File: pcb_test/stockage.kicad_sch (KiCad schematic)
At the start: 53 parts, among them U6 IS21EF08G-JCLI, U7 MX66LM1G45GXDI00

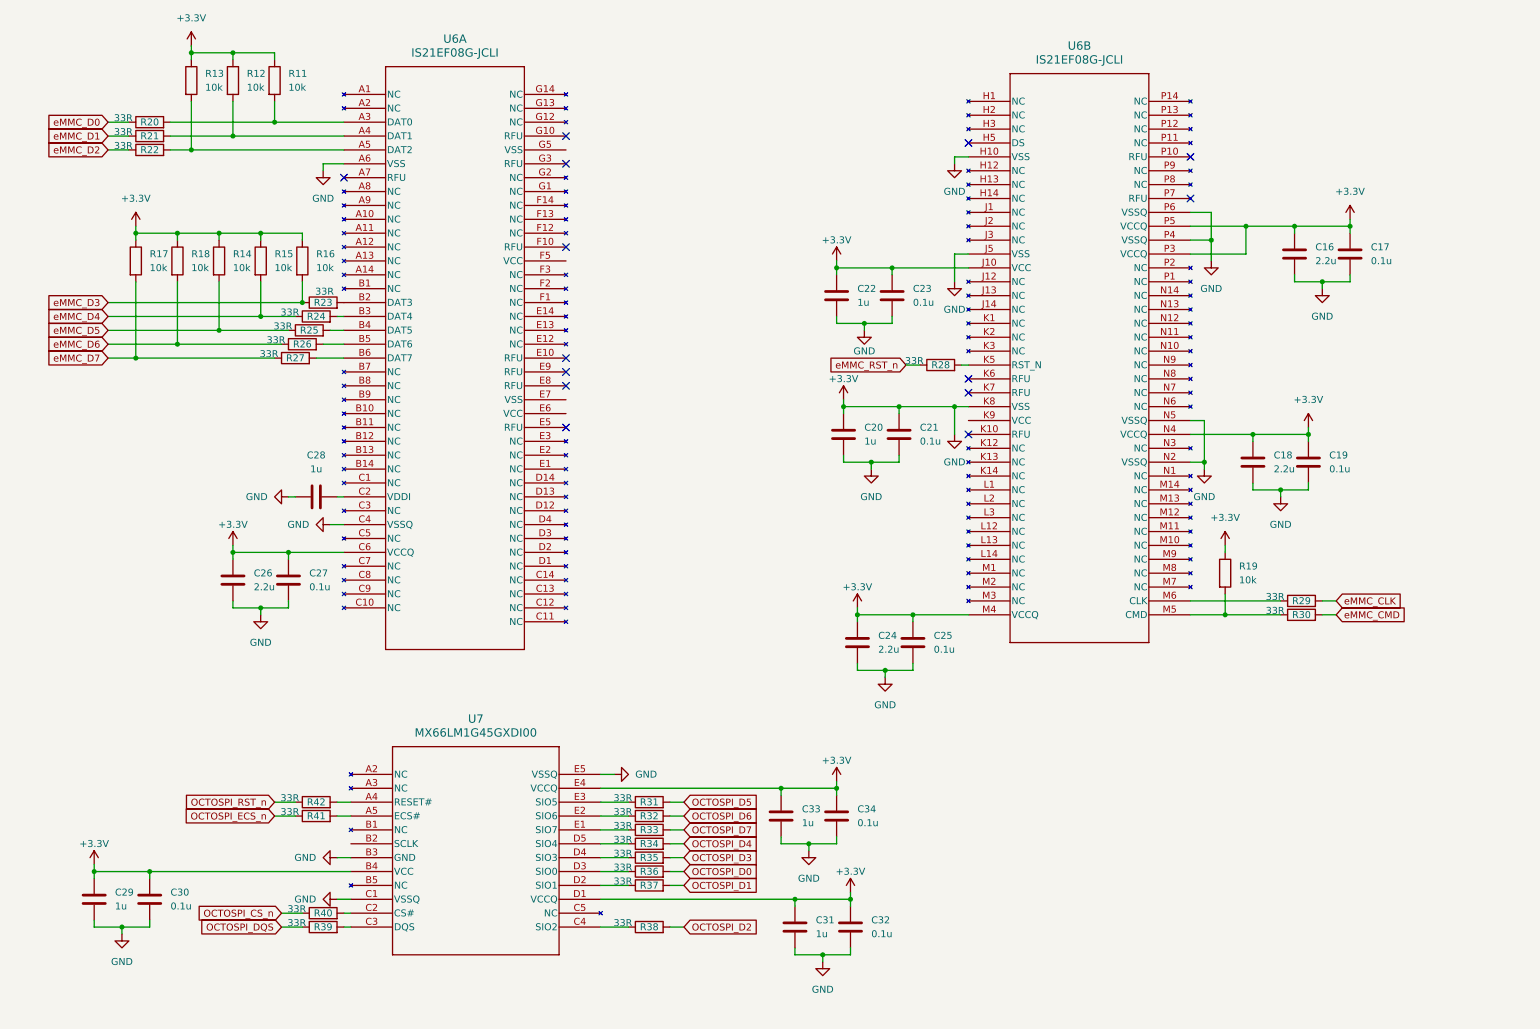
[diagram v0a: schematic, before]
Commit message: Ajout GPS, retrait radio, clean up schemas
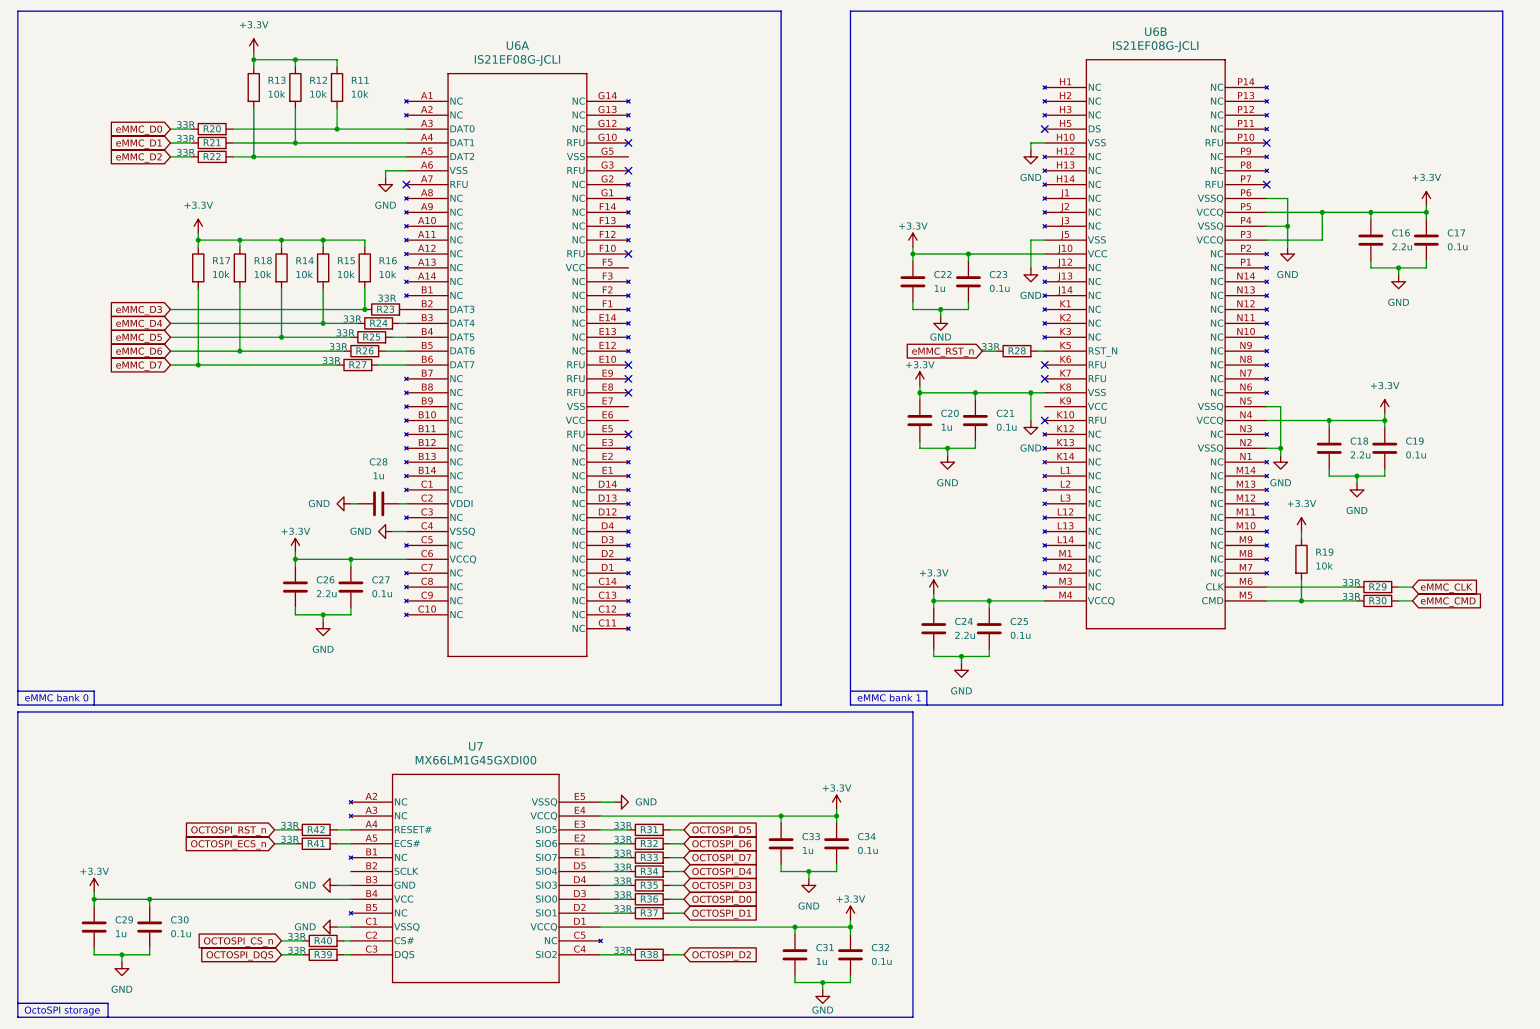
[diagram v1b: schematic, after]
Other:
- note added: "OctoSPI storage"
- note added: "eMMC bank 0"
- note added: "eMMC bank 1"
- moved on the sheet: C16, C17, C18, C19, C20, C21, C22, C23, C24, C25, C26, C27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

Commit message: Ajout testpoints
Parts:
- added R55: 10k, symbol Device:R
- added R56: 33R, symbol Device:R
- added TP19, TP20, TP21, TP22, TP23, TP24, TP25, TP26, TP27, TP28, TP29, TP30, TP31, TP32, TP33, TP34, TP35, TP36, TP37, TP38, TP39, TP40, TP41, TP42, TP43: TestPoint, symbol Connector:TestPoint
- R41: value 33R -> 10k
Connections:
- net OCTOSPI_ECS_n is gone; now on net +3.3V: R41.1
- net +3.3V: now also R55.1, TP42.1, TP43.1
- net OCTOSPI_CS_n: now also R55.2, TP21.1
- net OCTOSPI_D0: now also TP23.1
- net OCTOSPI_D1: now also TP24.1
- net OCTOSPI_D2: now also TP25.1
- net OCTOSPI_D3: now also TP26.1
- net OCTOSPI_D4: now also TP27.1
- net OCTOSPI_D5: now also TP28.1
- net OCTOSPI_D6: now also TP29.1
- net OCTOSPI_D7: now also TP30.1
- net OCTOSPI_DQS: now also TP22.1
- net OCTOSPI_RST_n: now also R56.1, TP19.1, TP20.1
- net eMMC_CLK: now also TP40.1
- net eMMC_CMD: now also TP41.1
- net eMMC_D0: now also TP31.1
- net eMMC_D1: now also TP32.1
- net eMMC_D2: now also TP33.1
- net eMMC_D3: now also TP34.1
- net eMMC_D4: now also TP35.1
- net eMMC_D5: now also TP36.1
- net eMMC_D6: now also TP37.1
- net eMMC_D7: now also TP38.1
- net eMMC_RST_n: now also TP39.1
- net at U7.B2 (SCLK): now also R56.2
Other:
- moved on the sheet: C29, C30

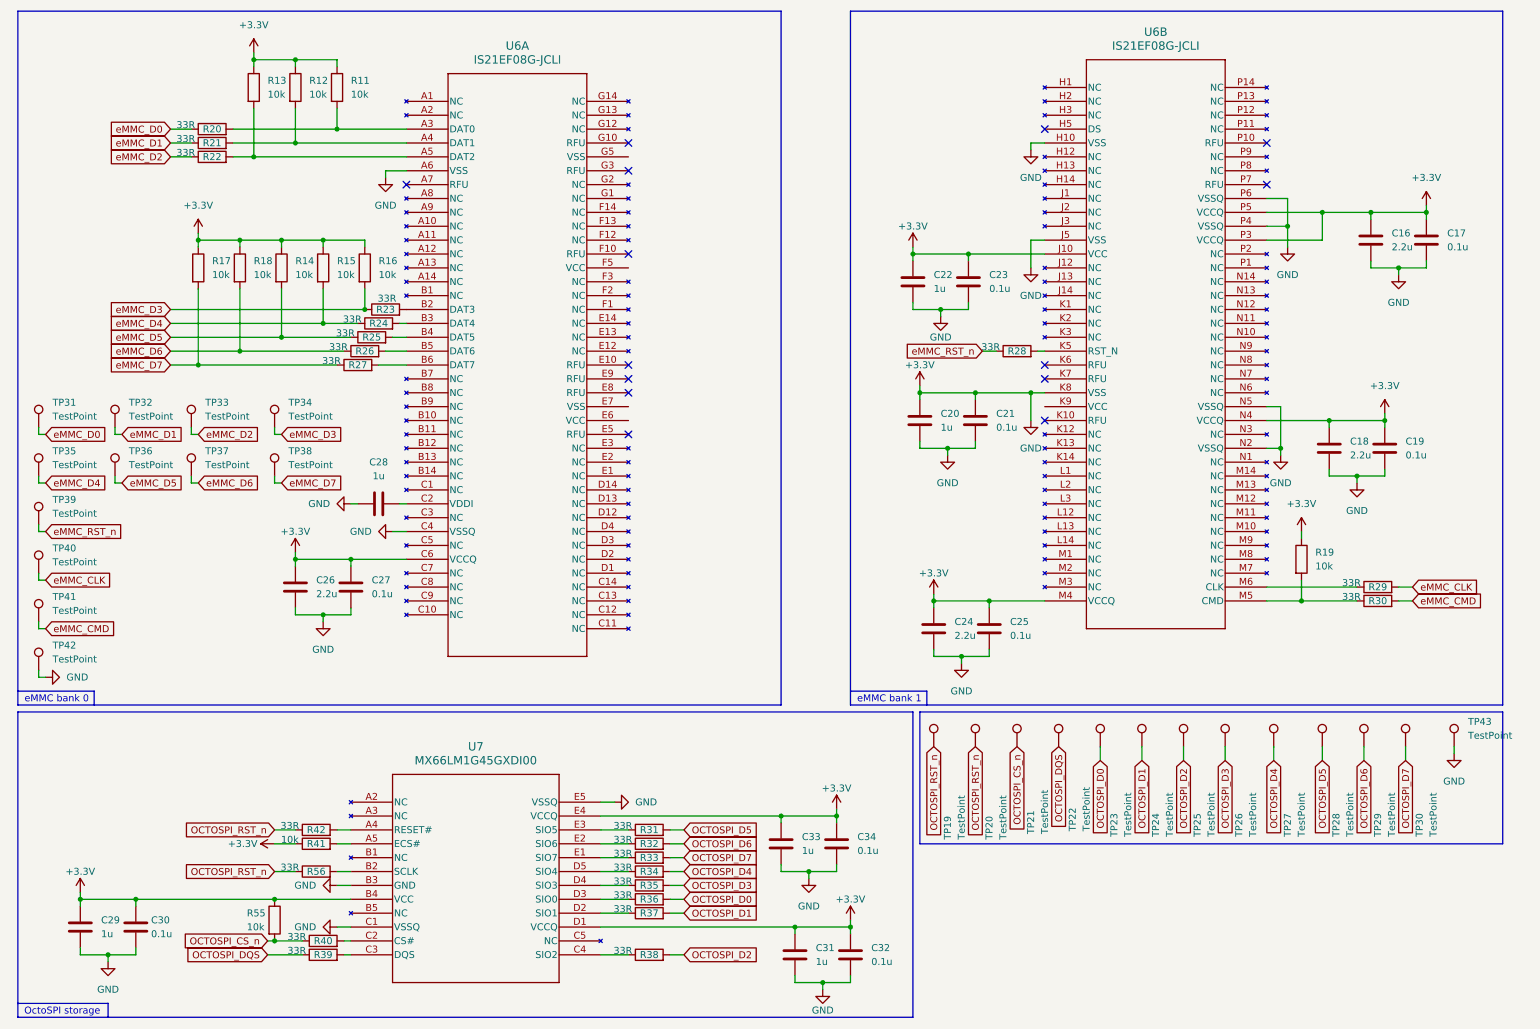
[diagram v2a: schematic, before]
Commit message: refait alimentation, changement MCU, separation schema eMMC/octospi, reajout RF
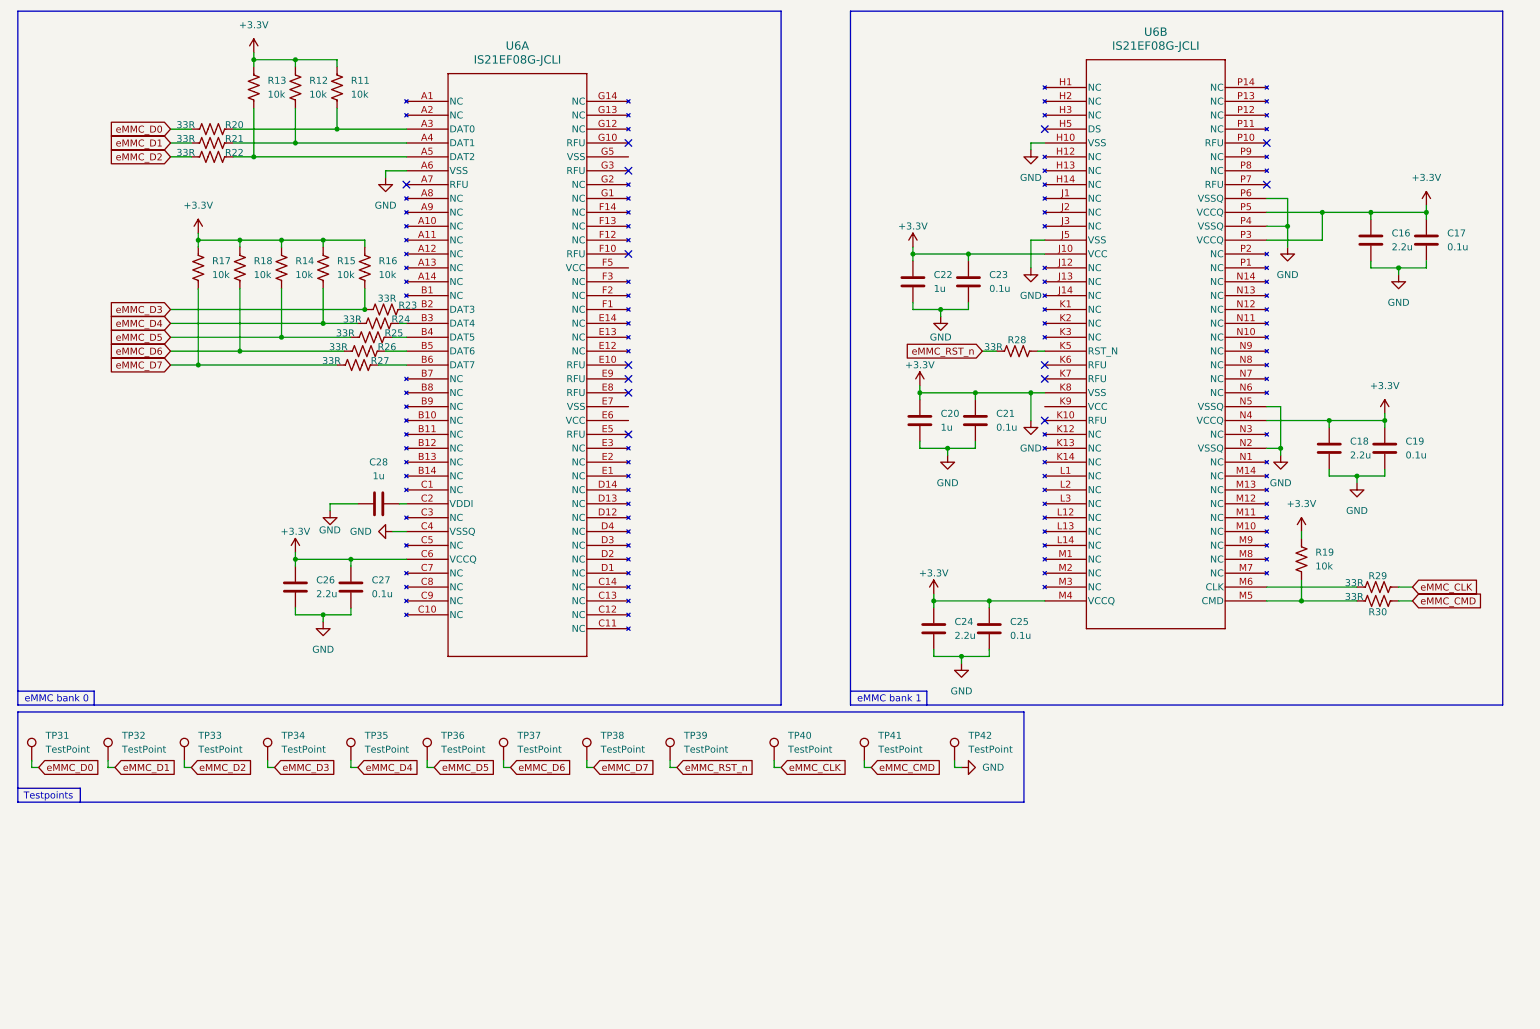
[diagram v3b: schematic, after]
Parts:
- removed C29, C31, C33: 1u, symbol Device:C
- removed C30, C32, C34: 0.1u, symbol Device:C
- removed R31, R32, R33, R34, R35, R36, R37, R38, R39, R40, R42, R56: 33R, symbol Device:R
- removed R41, R55: 10k, symbol Device:R
- removed TP19, TP20, TP21, TP22, TP23, TP24, TP25, TP26, TP27, TP28, TP29, TP30, TP43: TestPoint, symbol Connector:TestPoint
- removed U7: MX66LM1G45GXDI00, MX66LM1G:CSP24BGA_MAC-M, symbol MX66LM1G:MX66LM1G45GXDI00
- R11, R12, R13, R14, R15, R16, R17, R18, R19, R20, R21, R22, R23, R24, R25, R26, R27, R28, R29, R30: symbol Device:R -> Device:R_US
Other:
- note added: "Testpoints"
- note removed: "OctoSPI storage"
- moved on the sheet: TP31, TP32, TP33, TP34, TP35, TP36, TP37, TP38, TP39, TP40, TP41, TP42

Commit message: alimentation finale. Retouches testpoints et condo decouplage, finalisation requis, ajout sheet finale.
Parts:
- C16, C18, C20, C22, C24, C26: now not fitted
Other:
- moved on the sheet: C17, C19, C21, C23, C25, R19, R28, R29, R30, U6B
